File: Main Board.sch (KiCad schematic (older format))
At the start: 0 parts

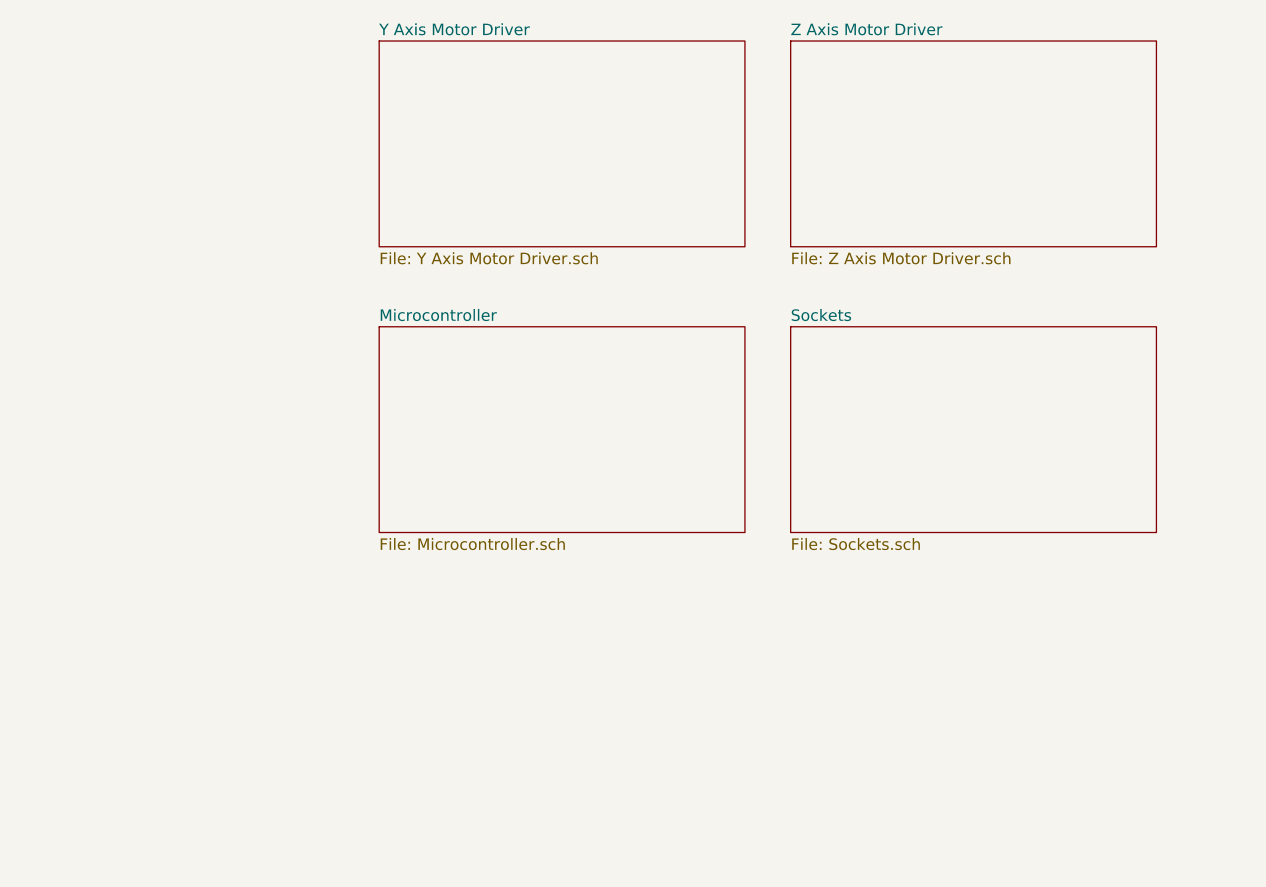
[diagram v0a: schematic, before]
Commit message: Finished TMC2209 schematic for Y and Z motor, added BOM
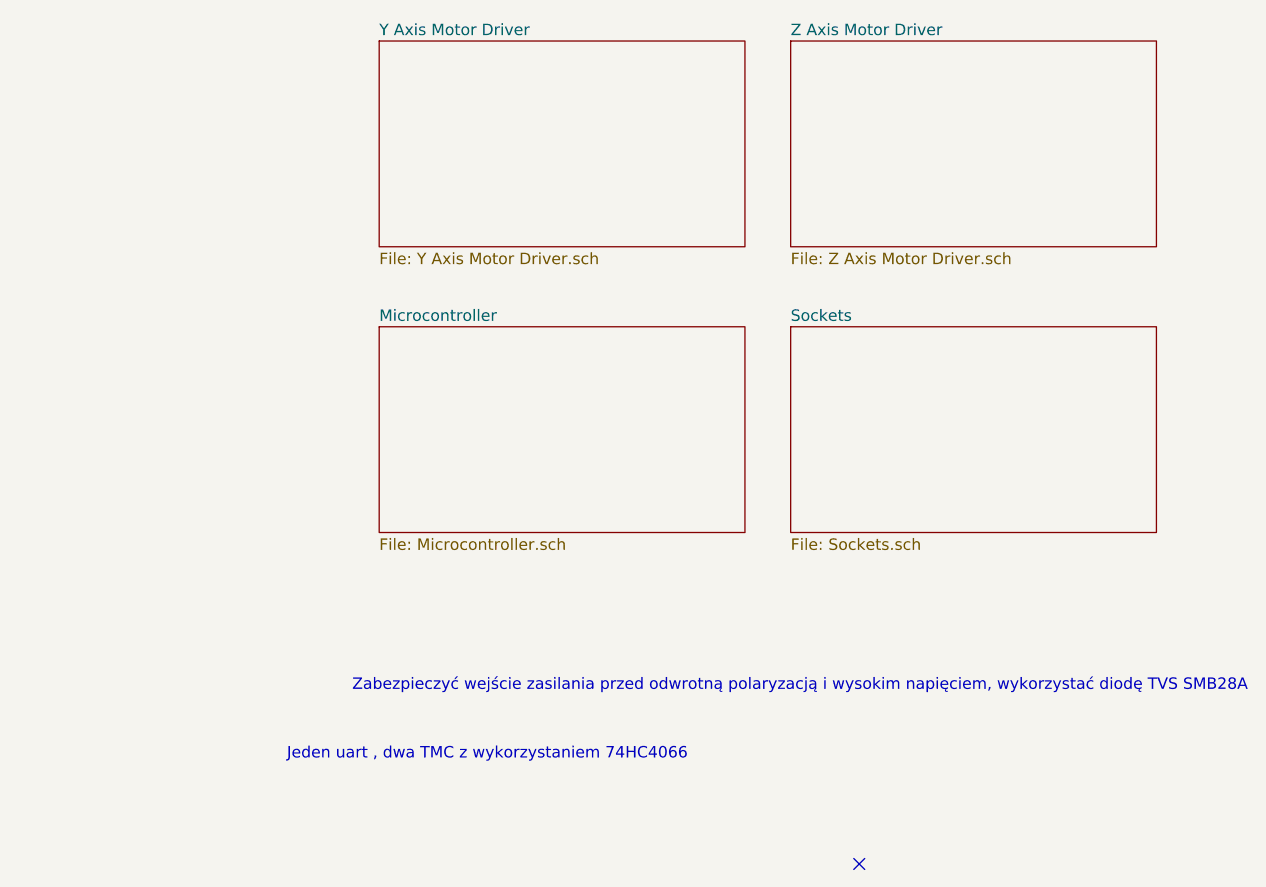
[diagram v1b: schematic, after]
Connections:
- no-connect marks 0 -> 1
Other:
- note added: "Jeden uart , dwa TMC z wykorzystaniem 74HC4066\n"
- note added: "Zabezpieczyć wejście zasilania przed odwrotną polaryzacją i wysokim napięciem, wykorzystać diodę TVS SMB28A"
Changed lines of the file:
@@
 F1 "Sockets.sch" 50
 $EndSheet
+Text Notes 5550 3650 2    50   ~ 0
+Zabezpieczyć wejście zasilania przed odwrotną polaryzacją i wysokim napięciem, wykorzystać diodę TVS SMB28A
+NoConn ~ 3850 4400
+Text Notes 3100 3950 2    50   ~ 0
+Jeden uart , dwa TMC z wykorzystaniem 74HC4066\n
 $EndSCHEMATC
